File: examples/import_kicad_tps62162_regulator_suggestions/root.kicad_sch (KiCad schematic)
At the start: 4 parts, among them U1 GENERIC_MCU

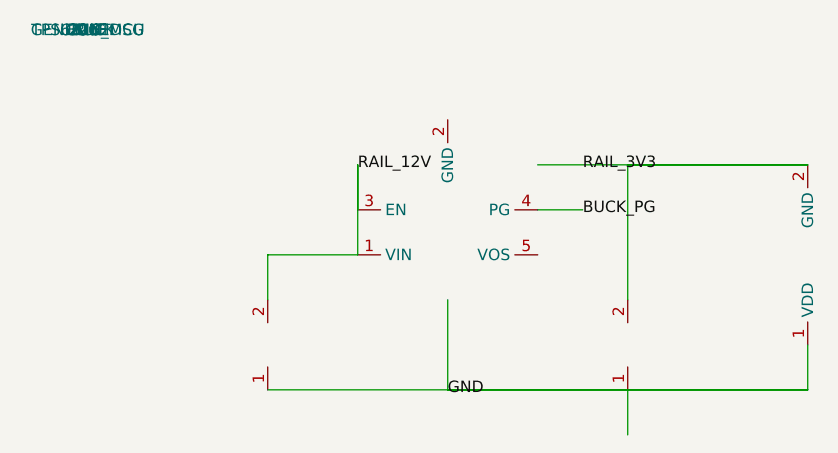
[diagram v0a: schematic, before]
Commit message: Validate buck output inductance
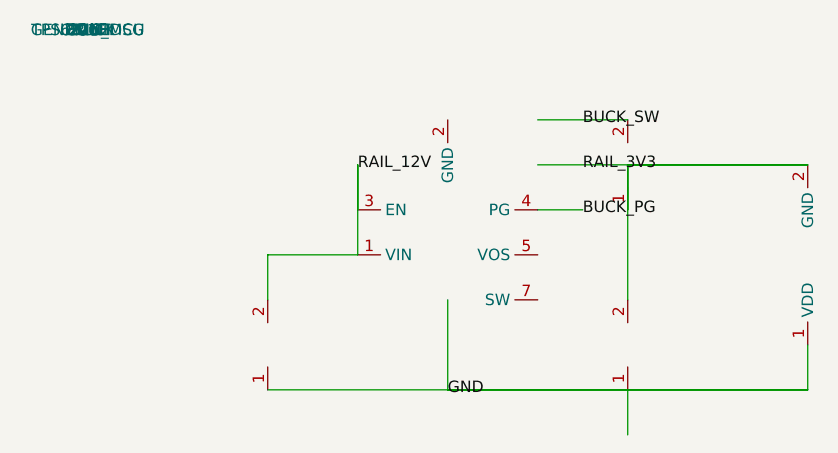
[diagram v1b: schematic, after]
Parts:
- added L1: 2.2uH, symbol Device:L
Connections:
- net RAIL_3V3: now also L1.1
- new net BUCK_SW: L1.2
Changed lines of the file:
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@@
     (property "Reference" "UBUCK")
     (property "Value" "TPS62162DSG")
-    (pin "1") (pin "2") (pin "3") (pin "4") (pin "5"))
+    (pin "1") (pin "2") (pin "3") (pin "4") (pin "5") (pin "7"))
   (symbol (lib_id "MCU:Generic") (at 80 25 0)
     (property "Reference" "U1")
@@
     (property "Value" "22uF")
     (pin "1") (pin "2"))
+  (symbol (lib_id "Device:L") (at 60 15 0)
+    (property "Reference" "L1")
+    (property "Value" "2.2uH")
+    (pin "1") (pin "2"))
   (wire (pts (xy 30 15) (xy 30 25) (xy 20 25) (xy 20 30)))
   (wire (pts (xy 30 20) (xy 30 15)))
   (label "RAIL_12V" (at 30 15 0))
   (wire (pts (xy 50 15) (xy 80 15) (xy 60 15) (xy 60 30)))
+  (wire (pts (xy 50 10) (xy 60 10)))
+  (label "BUCK_SW" (at 55 10 0))
+  (wire (pts (xy 60 20) (xy 60 15)))
   (label "RAIL_3V3" (at 55 15 0))
   (wire (pts (xy 50 20) (xy 55 20)))
